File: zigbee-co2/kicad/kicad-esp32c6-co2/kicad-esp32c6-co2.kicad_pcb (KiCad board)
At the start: 2 copper layers, 1 part, among them U1 XIAO-ESP32-C6-DIP

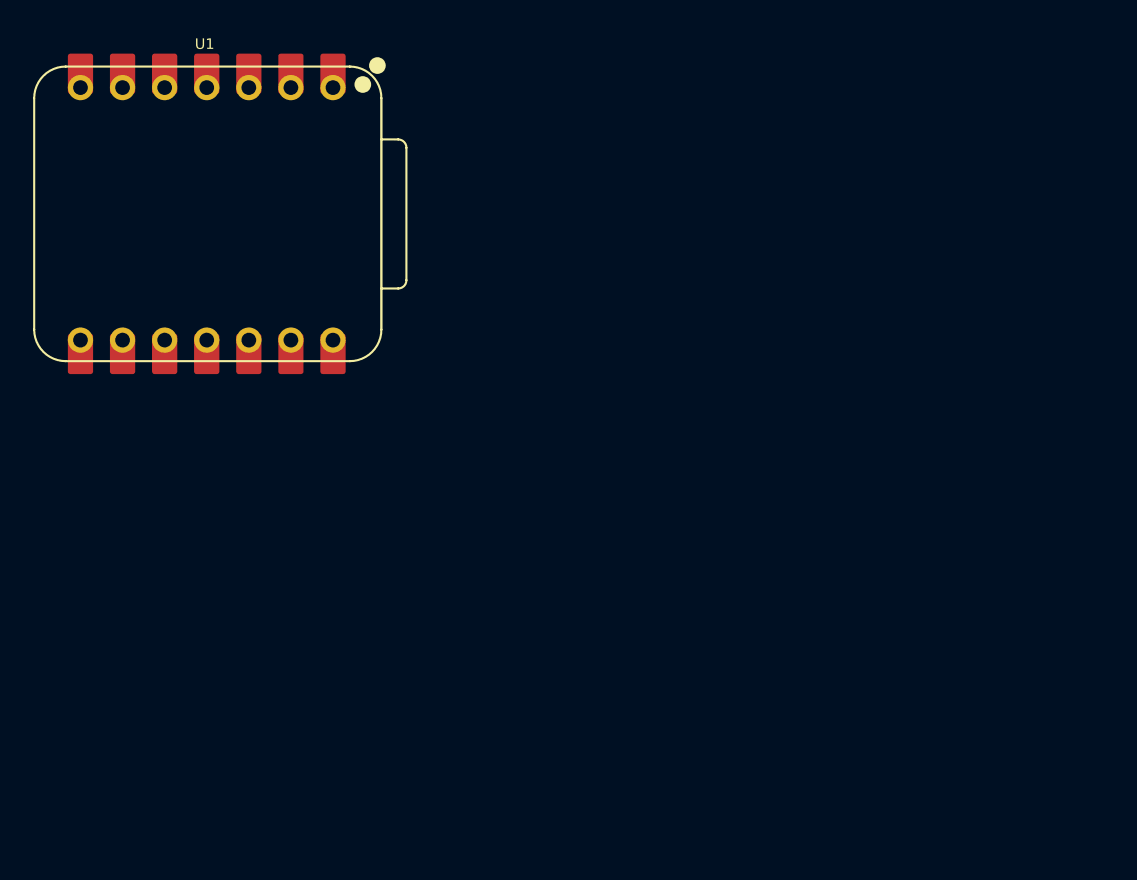
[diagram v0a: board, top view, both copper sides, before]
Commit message: feat: configure PCB stackup and add custom footprint library for 4-layer board
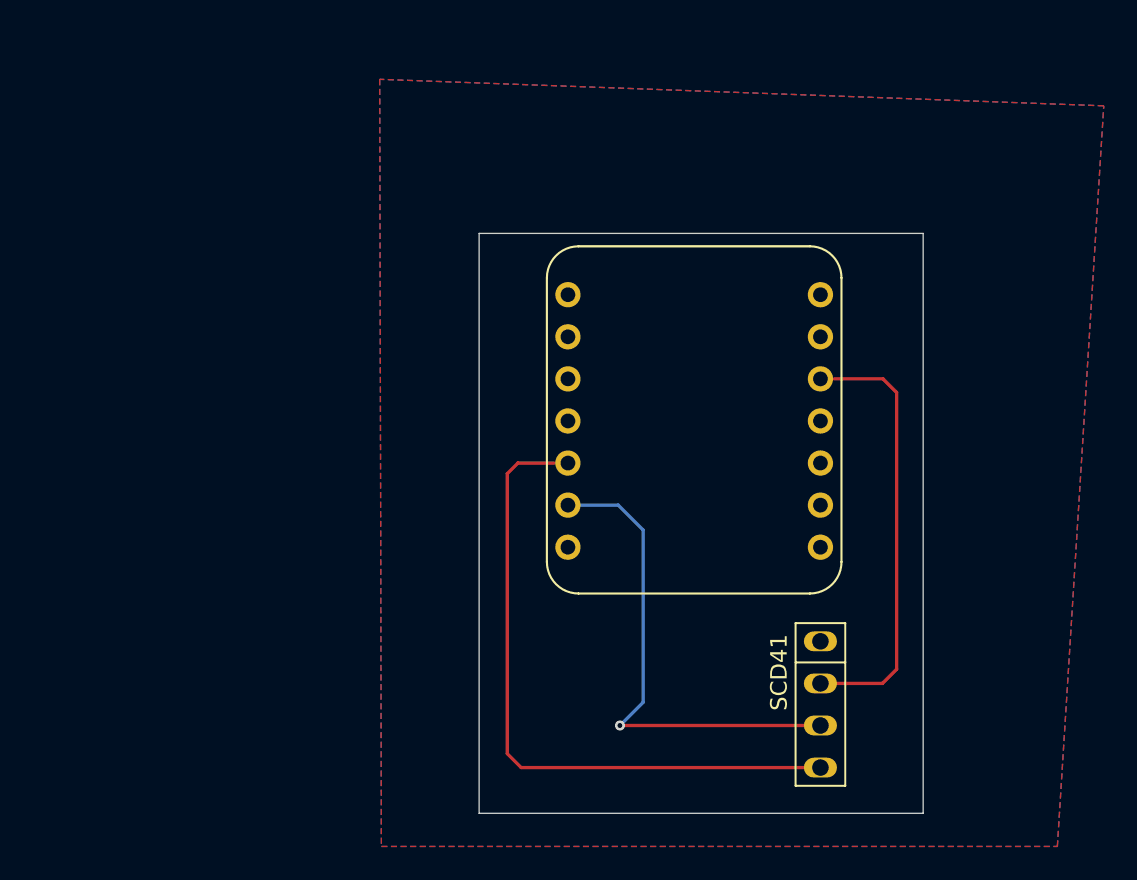
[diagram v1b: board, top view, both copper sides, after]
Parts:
- added SCD41: ~, Library:SCD41-4pins, F.Cu at (79.0, 67.7)
- U1: footprint seeds-studio:XIAO-ESP32-C6-DIP -> Library:XIAO-ESP32-C6-DIP
- moved U1 32.0 mm to (71.4, 50.6), turned to 90 degrees
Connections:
- U1 pad 12: unconnected-(U1-3V3-Pad12) -> +3.3V
- U1 pad 5: unconnected-(U1-GPIO22/D4/SDA-Pad5) -> Net-(SCD41-SDA)
- U1 pad 6: unconnected-(U1-GPIO23/D5/SCL-Pad6) -> Net-(SCD41-SCL)
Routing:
- net Net-(SCD41-SDA): track 0.00 -> 39.2 mm
- net Net-(SCD41-SCL): track 0.00 -> 29.6 mm, vias 0 -> 1
- net +3.3V: track 0.00 -> 25.8 mm
- added copper zone on B.Cu, net GND
- added copper zone on F.Cu, net GND
- added copper zone on In1.Cu, net GND
- added copper zone on In2.Cu, net GND
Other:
- board outline added: 26.8 x 35 mm
- copper layers 2 -> 4
